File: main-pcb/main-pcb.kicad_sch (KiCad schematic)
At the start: 0 parts

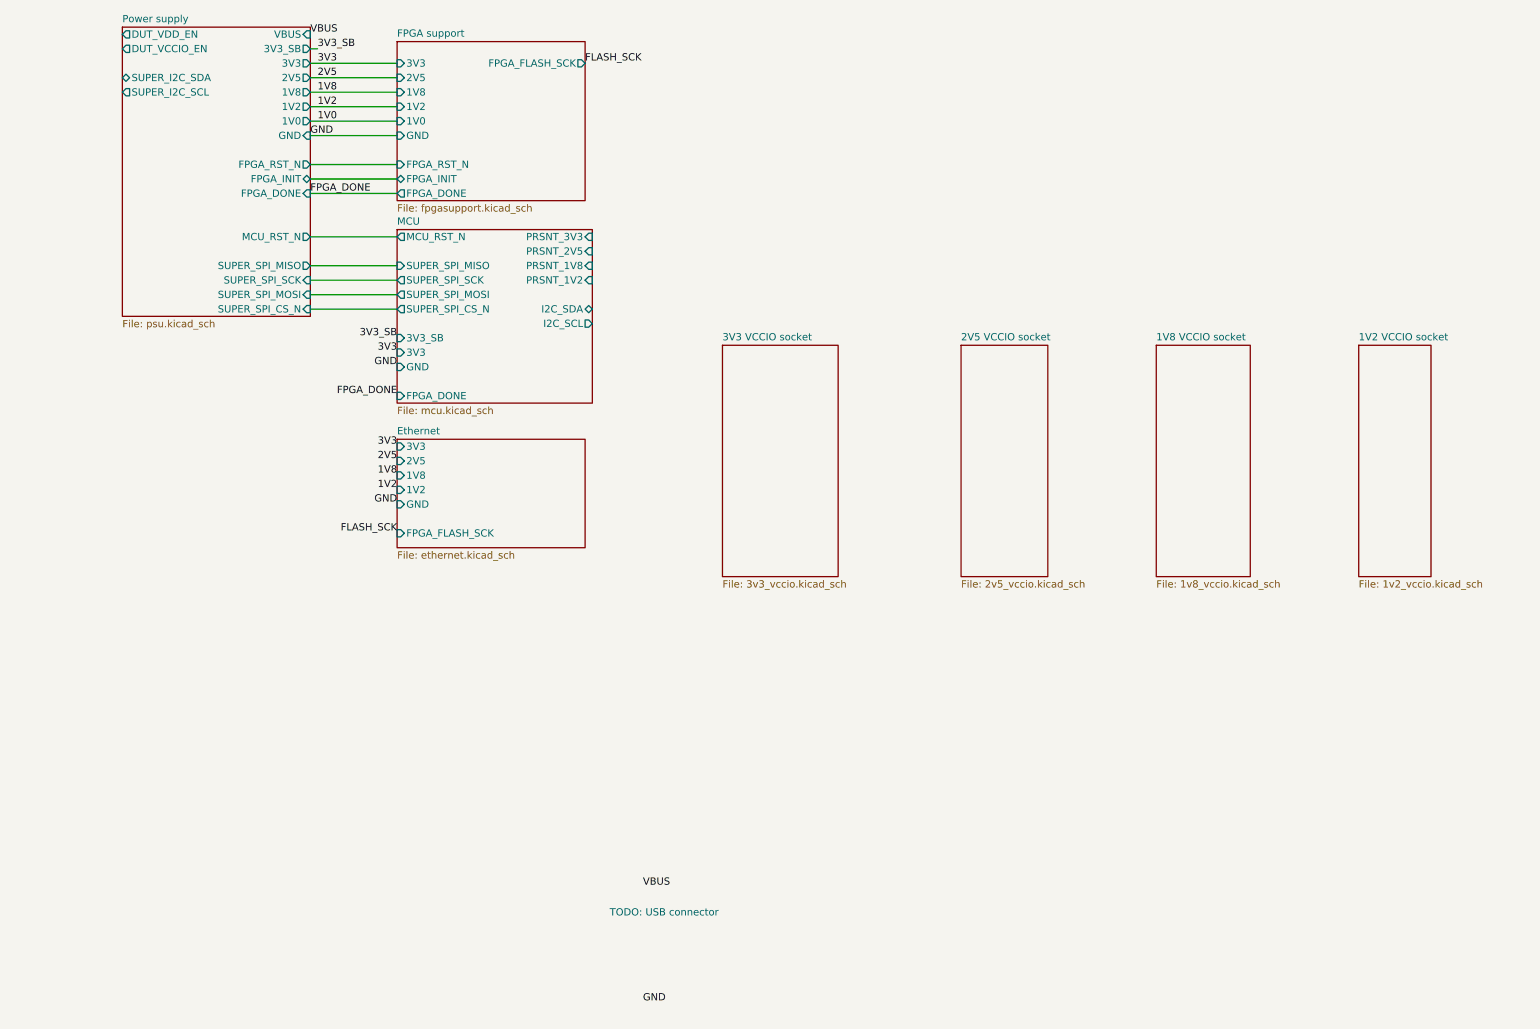
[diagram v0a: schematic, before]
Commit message: Initial design mostly done aside from USB connector, review, test points
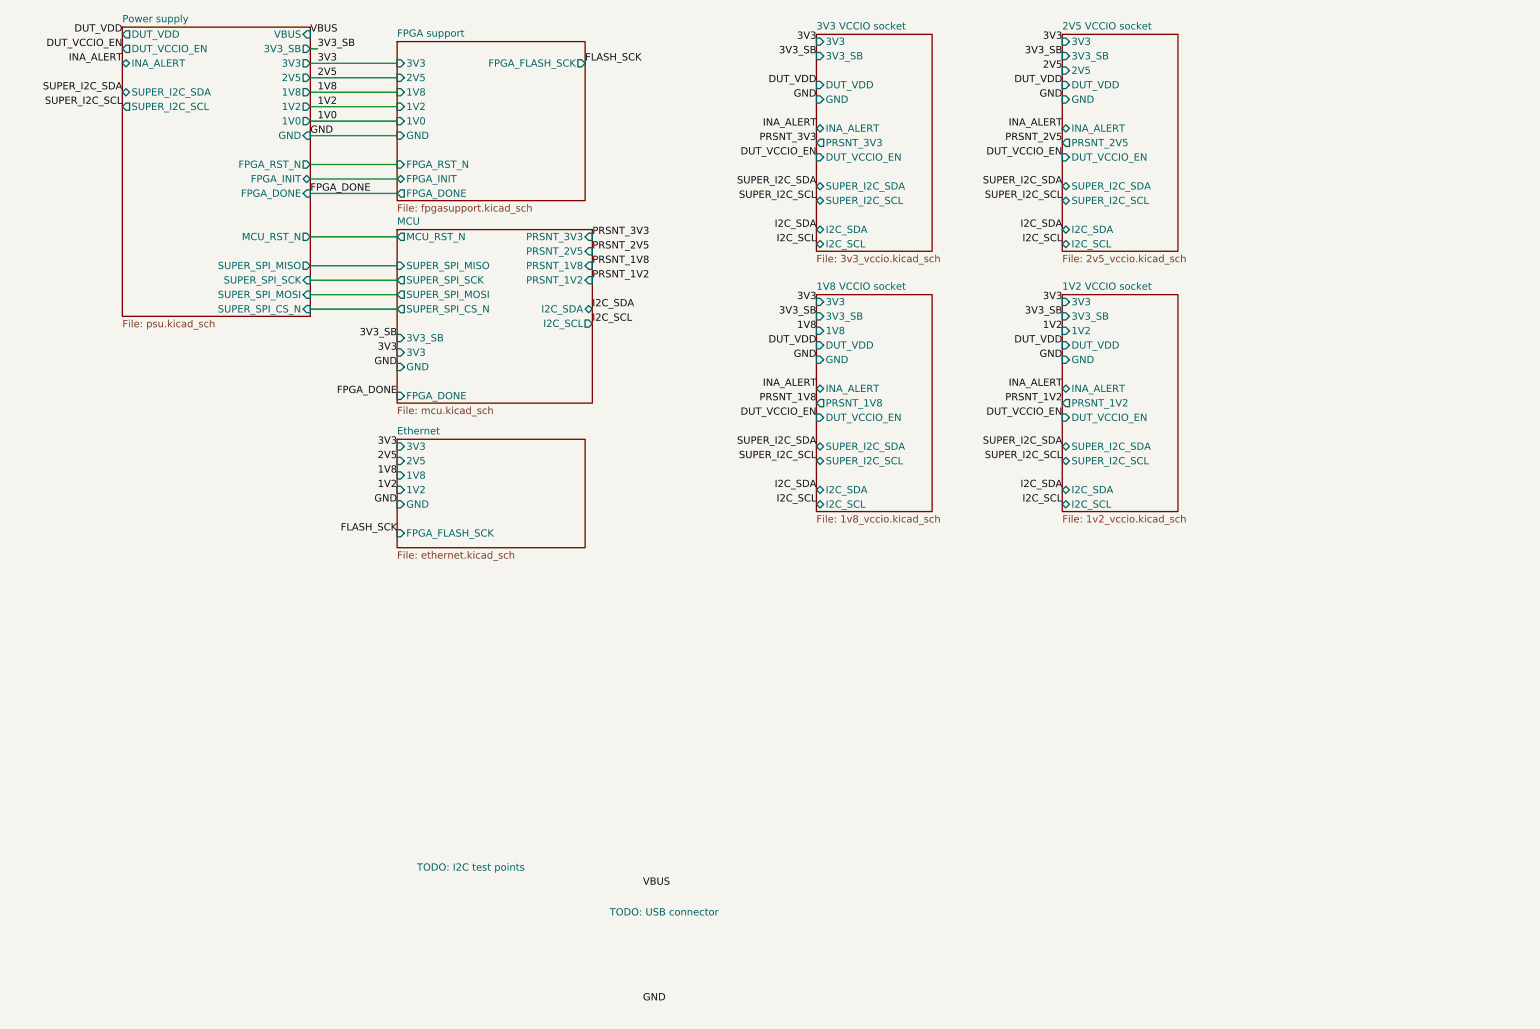
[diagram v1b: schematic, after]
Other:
- sheet 1V2 VCCIO socket ports: added 1V2, 3V3, 3V3_SB, DUT_VCCIO_EN, DUT_VDD, GND, I2C_SCL, I2C_SDA, INA_ALERT, PRSNT_1V2, SUPER_I2C_SCL, SUPER_I2C_SDA; removed none
- sheet 1V8 VCCIO socket ports: added 1V8, 3V3, 3V3_SB, DUT_VCCIO_EN, DUT_VDD, GND, I2C_SCL, I2C_SDA, INA_ALERT, PRSNT_1V8, SUPER_I2C_SCL, SUPER_I2C_SDA; removed none
- sheet 2V5 VCCIO socket ports: added 2V5, 3V3, 3V3_SB, DUT_VCCIO_EN, DUT_VDD, GND, I2C_SCL, I2C_SDA, INA_ALERT, PRSNT_2V5, SUPER_I2C_SCL, SUPER_I2C_SDA; removed none
- sheet 3V3 VCCIO socket ports: added 3V3, 3V3_SB, DUT_VCCIO_EN, DUT_VDD, GND, I2C_SCL, I2C_SDA, INA_ALERT, PRSNT_3V3, SUPER_I2C_SCL, SUPER_I2C_SDA; removed none
- sheet Power supply ports: added DUT_VDD, INA_ALERT; removed DUT_VDD_EN
- note added: "TODO: I2C test points"

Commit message: Finished initial schematic pass, ready for review
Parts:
- added F1: 1A, symbol power-azonenberg:FUSE_PWROUT_2
- added J14: USB_C_Receptacle_USB2.0, Connector_USB:USB_C_Receptacle_HRO_TYPE-C-31-M-12, symbol lain:USB_C_Receptacle_USB2.0
- added L8: BLM31KN271SN1L, symbol passive-azonenberg:INDUCTOR_PWROUT
- added R103, R104: 5.1k, symbol device:R
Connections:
- net GND: now also J14.A1 (GND), J14.A12 (GND), J14.B1 (GND), J14.B12 (GND), J14.S1 (SHIELD), R103.2, R104.2
- net VBUS: now also L8.1
- new net: J14.B5 (CC2), R103.1
- new net: F1.2, L8.2
- new net: F1.1, J14.A4 (VBUS), J14.A9 (VBUS), J14.B4 (VBUS), J14.B9 (VBUS)
- new net: J14.A5 (CC1), R104.1
- new net: J14.A6 (D+), J14.B6 (D+)
- new net: J14.A7 (D-), J14.B7 (D-)
- no-connect marks 0 -> 2
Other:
- note removed: "TODO: USB connector"

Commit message: More schematic tweaks and test points
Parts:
- F1, R103, R104: footprint (none) -> azonenberg_pcb:EIA_0402_RES_NOSILK
- L8: footprint (none) -> azonenberg_pcb:EIA_1206_CAP_NOSILK
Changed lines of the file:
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@@
 			)
 		)
-		(property "Footprint" ""
+		(property "Footprint" "azonenberg_pcb:EIA_0402_RES_NOSILK"
 			(at 60.96 137.668 90)
 			(effects
@@
 			)
 		)
-		(property "Footprint" ""
+		(property "Footprint" "azonenberg_pcb:EIA_1206_CAP_NOSILK"
 			(at 86.36 128.27 0)
 			(effects
@@
 					(size 1.524 1.524)
 				)
+				(hide yes)
 			)
 		)
@@
 			)
 		)
-		(property "Footprint" ""
+		(property "Footprint" "azonenberg_pcb:EIA_0402_RES_NOSILK"
 			(at 66.675 128.27 0)
 			(effects
@@
 					(size 1.524 1.524)
 				)
+				(hide yes)
 			)
 		)
@@
 			)
 		)
-		(property "Footprint" ""
+		(property "Footprint" "azonenberg_pcb:EIA_0402_RES_NOSILK"
 			(at 60.96 135.128 90)
 			(effects

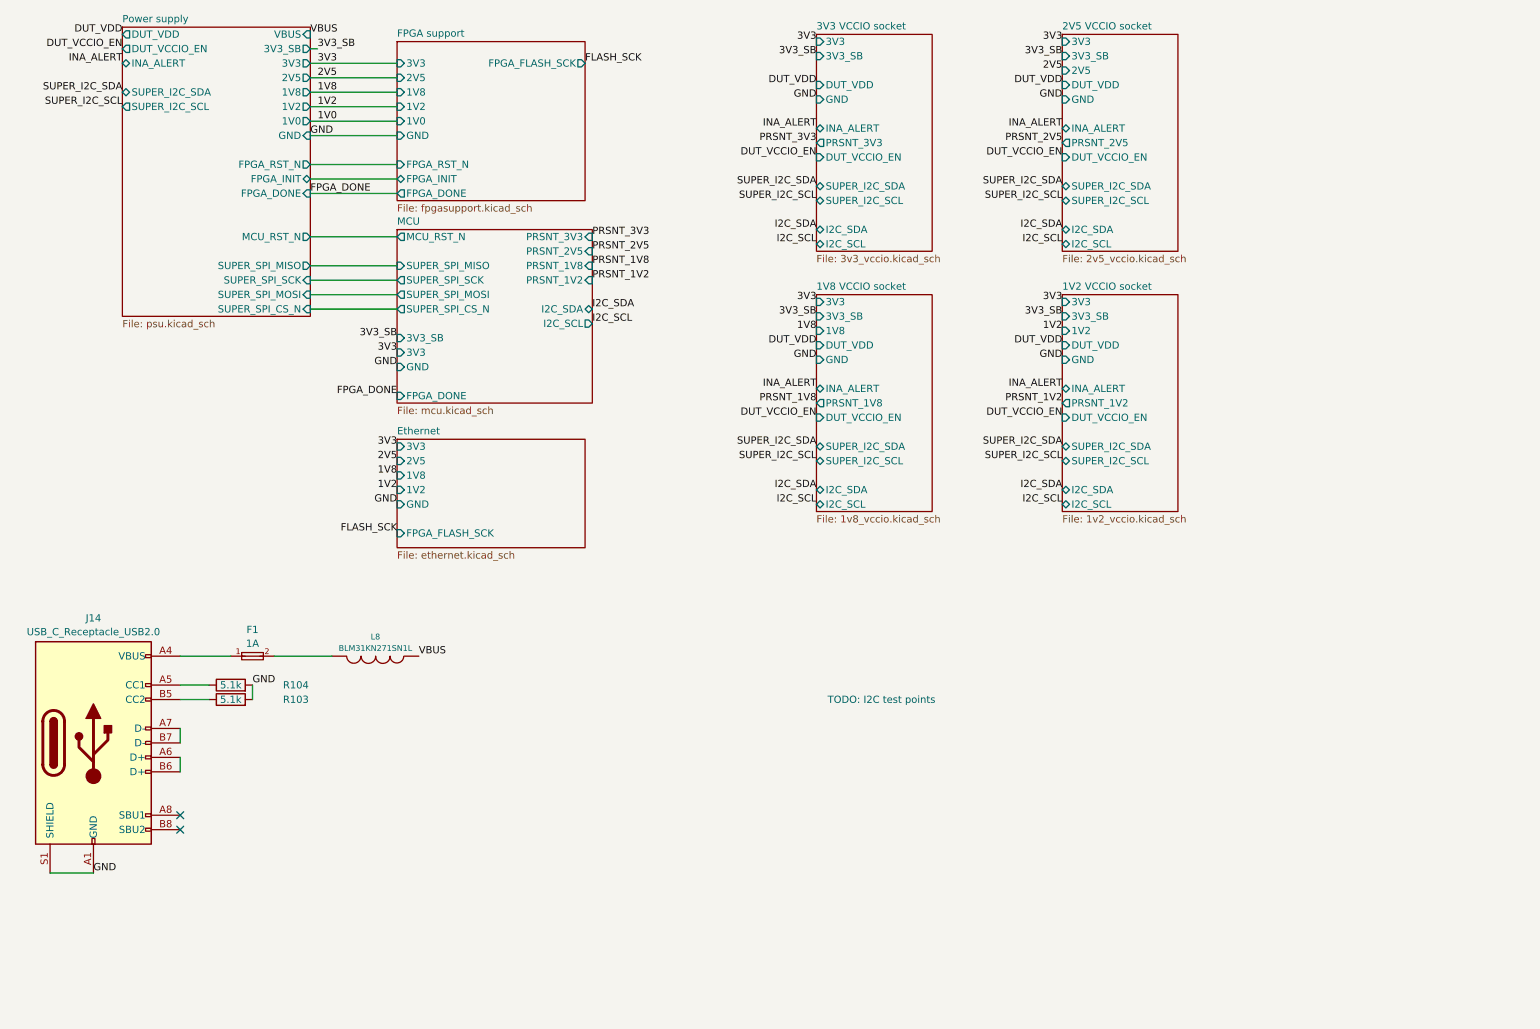
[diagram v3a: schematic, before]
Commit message: Added some RGB LEDs, changed a few voltage dividers to match what was in stock. Time for next round of review.
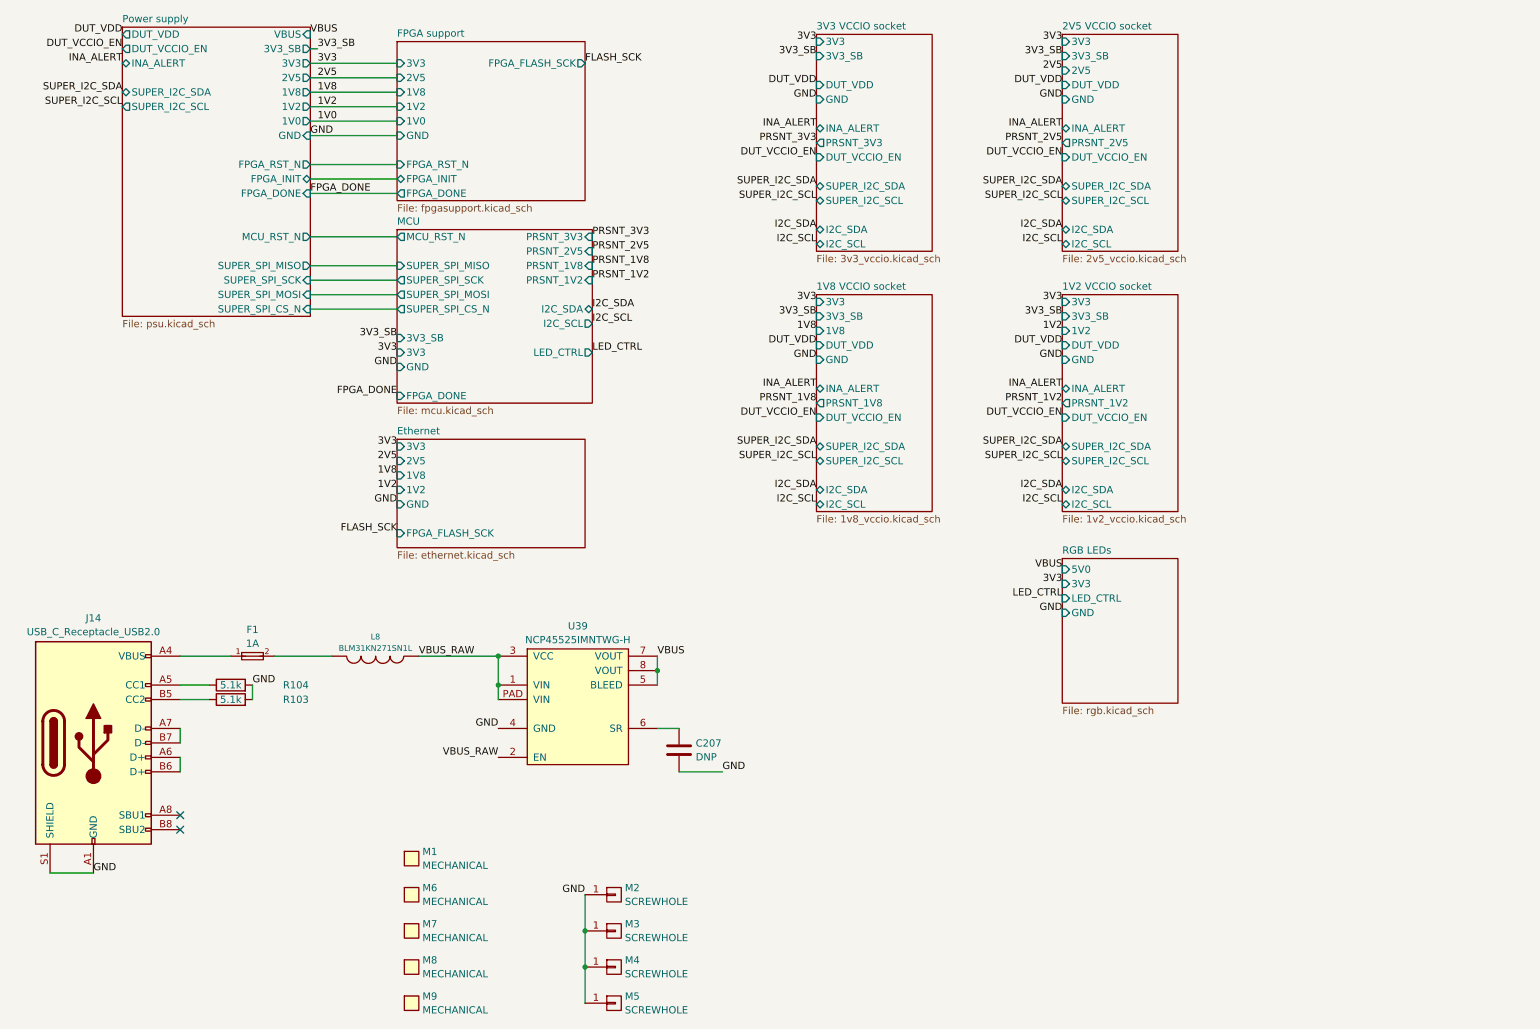
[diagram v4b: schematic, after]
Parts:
- added C207: DNP, azonenberg_pcb:EIA_0402_CAP_NOSILK, symbol device:C
- added M1: MECHANICAL, azonenberg_pcb:LONGTHING-1200DPI, symbol special-azonenberg:MECHANICAL
- added M2, M3, M4, M5: SCREWHOLE, azonenberg_pcb:MECHANICAL_CLEARANCEHOLE_4_40, symbol conn:CONN_01X01
- added M6: MECHANICAL, azonenberg_pcb:LOGO_ESD_SENSITIVE_7MM, symbol special-azonenberg:MECHANICAL
- added M7: MECHANICAL, w_logo:Logo_silk_OSHW_6x6mm, symbol special-azonenberg:MECHANICAL
- added M8: MECHANICAL, w_logo:Logo_silk_ROHS_5x2.8mm, symbol special-azonenberg:MECHANICAL
- added M9: MECHANICAL, w_logo:Logo_silk_WEEE_3.4x5mm, symbol special-azonenberg:MECHANICAL
- added U39: NCP45525IMNTWG-H, azonenberg_pcb:DFN_8_0.5MM_2x2MM, symbol power-azonenberg:NCP45525
- J14: footprint Connector_USB:USB_C_Receptacle_HRO_TYPE-C-31-M-12 -> lain:GCT_USB4500-03-0-A
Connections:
- net GND: now also C207.2, M2.1 (P1), M3.1 (P1), M4.1 (P1), M5.1 (P1), U39.4 (GND)
- net VBUS: now also U39.5 (BLEED), U39.7 (VOUT), U39.8 (VOUT); no longer L8.1
- new net: C207.1, U39.6 (SR)
- new net VBUS_RAW: L8.1, U39.1 (VIN), U39.2 (EN), U39.3 (VCC), U39.PAD (VIN)
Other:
- added sheet RGB LEDs (rgb.kicad_sch)
- sheet MCU ports: added LED_CTRL; removed none
- note removed: "TODO: I2C test points"

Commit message: Finished schematic review
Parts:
- added C208: 0.47 uF, azonenberg_pcb:EIA_0402_CAP_NOSILK, symbol device:C
- added TP18, TP19, TP20: GROUND, azonenberg_pcb:TESTPOINT_SMT_KEYSTONE_5016, symbol conn:CONN_01X01
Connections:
- net GND: now also C208.2, TP18.1 (P1), TP19.1 (P1), TP20.1 (P1)
- net VBUS_RAW: now also C208.1
- net at J14.A6 (D+): no longer J14.B6 (D+)
- net at J14.A7 (D-): no longer J14.B7 (D-)
- no-connect marks 2 -> 6
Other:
- sheet Power supply ports: added VBUS_SHOUT; removed none
